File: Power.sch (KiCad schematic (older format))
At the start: 40 parts, among them U1 LP2985-3.3, U3 LP2985-3.3, U4 MP4560_QFN10, U5 MP4560_QFN10

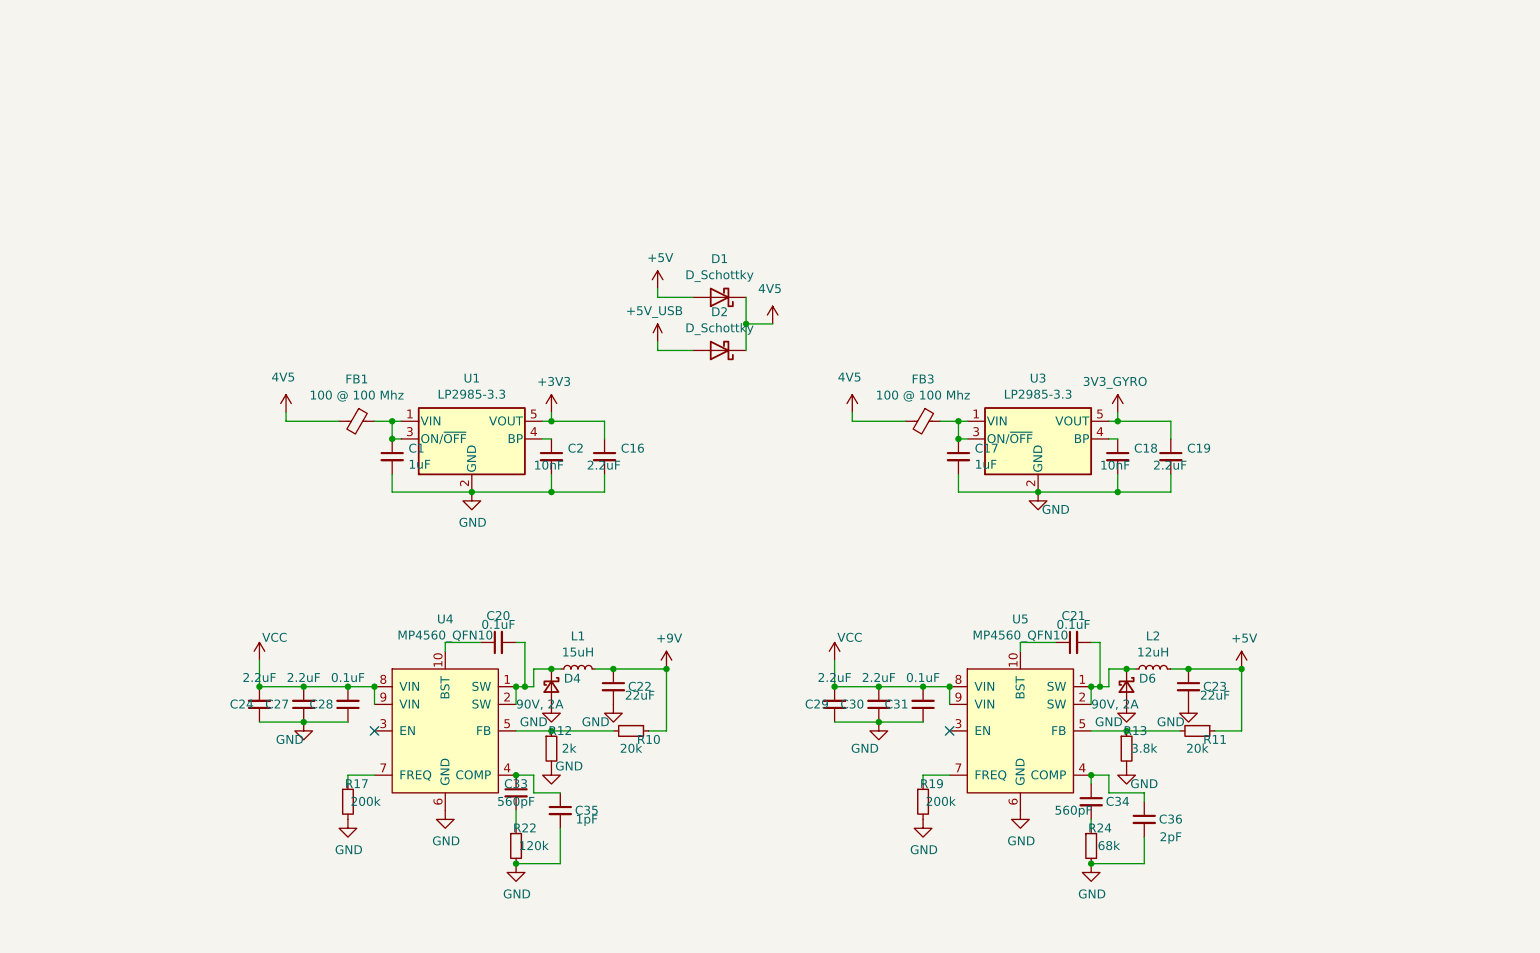
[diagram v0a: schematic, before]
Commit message: Updated the schematics to include pictures
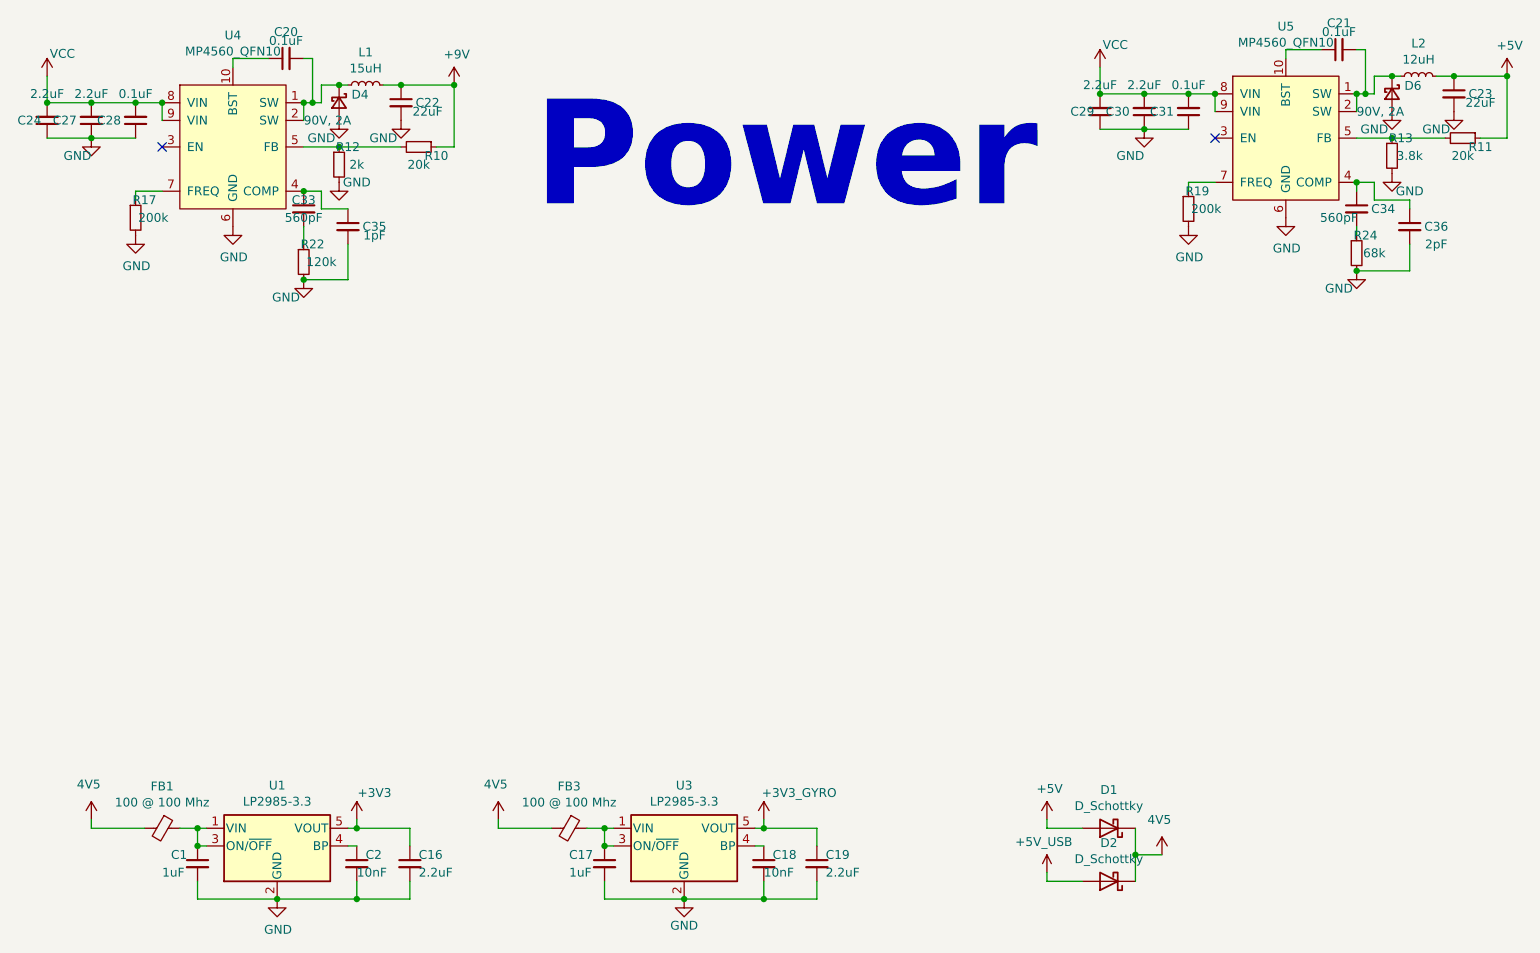
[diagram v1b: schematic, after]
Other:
- note added: "Power"
- moved on the sheet: C1, C16, C17, C18, C19, C2, C20, C21, C22, C23, C24, C27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

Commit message: Changed around routing
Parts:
- removed C27, C30: 2.2uF, Capacitor_SMD:C_0603_1608Metric, symbol Device:C_Small
- C24, C29: value 2.2uF -> 4.7uF
- C33, C34: value 560pF -> 390pF
- C36: value 2pF -> 1pF
- L1, L2: footprint Inductor_SMD:L_XGL4030 -> Inductor_SMD:L_Bourns-SRN3015
- R22: value 120k -> 165k
- R24: value 68k -> 93.1k
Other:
- moved on the sheet: C24, C29
